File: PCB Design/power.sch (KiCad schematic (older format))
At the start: 18 parts, among them CON2 BARREL_JACK, P1 Power Sel, U1 3.3VREG

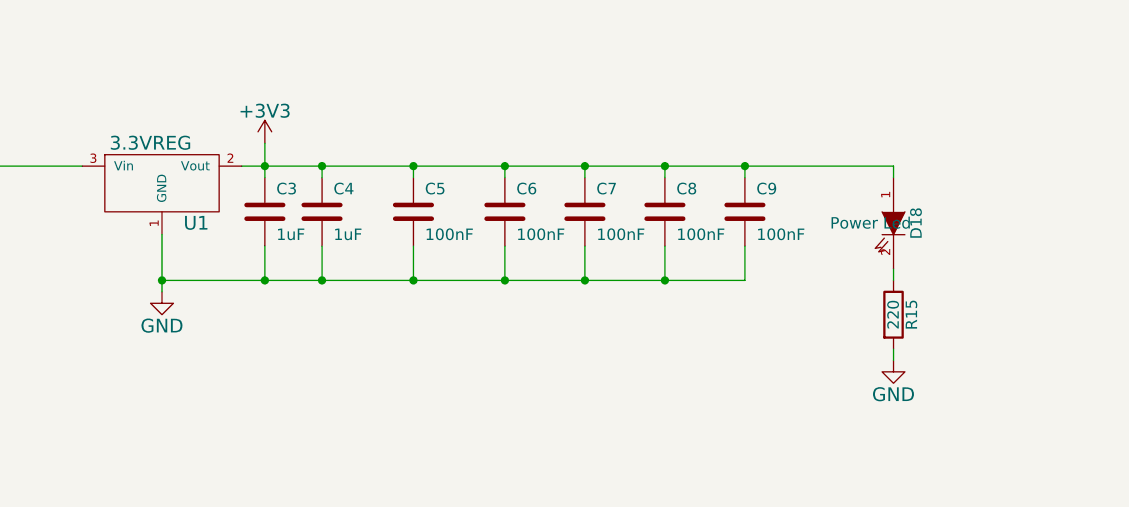
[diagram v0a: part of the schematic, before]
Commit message: Added an additional cap for the MCU, added copper fill on all layers.
Signed-off-by: Kolijn Wolfaardt <kolijn.wolfaardt@gmail.com>
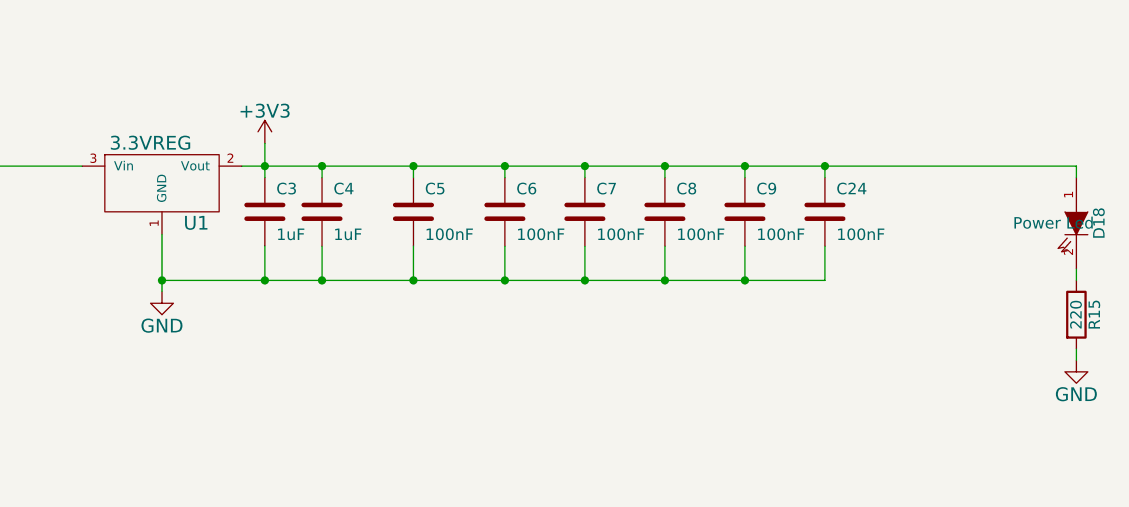
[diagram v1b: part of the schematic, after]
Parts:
- added C24: 100nF, Capacitors_SMD:C_1206, symbol C
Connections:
- net +3V3: now also C24.1
- net GND: now also C24.2
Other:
- moved on the sheet: D18, R15
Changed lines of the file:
@@
 $EndComp
 Wire Wire Line
-	6500 3900 9350 3900
+	6500 3900 10150 3900
 Wire Wire Line
 	6600 3800 6600 3950
@@
 $EndComp
 Wire Wire Line
-	6150 4450 6150 4200
+	6150 4200 6150 4450
 $Comp
 L C C1
@@
 $EndComp
 Wire Wire Line
-	8700 4400 6150 4400
+	6150 4400 9050 4400
 Wire Wire Line
 	6600 4250 6600 4400
@@
 Connection ~ 8000 4400
 Wire Wire Line
-	8700 4250 8700 4400
+	8700 4400 8700 4250
 Connection ~ 8350 4400
 Connection ~ 8350 3900
@@
 L LED D18
 U 1 1 551840ED
-P 9350 4150
-F 0 "D18" H 9350 4250 50  0000 C CNN
-F 1 "Power Led" V 9350 4050 50  0000 C CNN
-F 2 "LEDs:LED-1206" H 9350 4150 60  0001 C CNN
-F 3 "" H 9350 4150 60  0000 C CNN
-	1    9350 4150
+P 10150 4150
+F 0 "D18" H 10150 4250 50  0000 C CNN
+F 1 "Power Led" V 10150 4050 50  0000 C CNN
+F 2 "LEDs:LED-1206" H 10150 4150 60  0001 C CNN
+F 3 "" H 10150 4150 60  0000 C CNN
+	1    10150 4150
 	0    1    1    0
 $EndComp
@@
 L R R15
 U 1 1 55184149
-P 9350 4550
-F 0 "R15" V 9430 4550 50  0000 C CNN
-F 1 "220" V 9350 4550 50  0000 C CNN
-F 2 "Resistors_SMD:R_1206" V 9280 4550 30  0001 C CNN
-F 3 "" H 9350 4550 30  0000 C CNN
-	1    9350 4550
+P 10150 4550
+F 0 "R15" V 10230 4550 50  0000 C CNN
+F 1 "220" V 10150 4550 50  0000 C CNN
+F 2 "Resistors_SMD:R_1206" V 10080 4550 30  0001 C CNN
+F 3 "" H 10150 4550 30  0000 C CNN
+	1    10150 4550
 	1    0    0    -1
 $EndComp
@@
 L GND #PWR08
 U 1 1 551841D4
-P 9350 4750
-F 0 "#PWR08" H 9350 4500 60  0001 C CNN
-F 1 "GND" H 9350 4600 60  0000 C CNN
-F 2 "" H 9350 4750 60  0000 C CNN
-F 3 "" H 9350 4750 60  0000 C CNN
-	1    9350 4750
-	1    0    0    -1
-$EndComp
-Wire Wire Line
-	9350 4700 9350 4750
-Wire Wire Line
-	9350 4400 9350 4350
-Wire Wire Line
-	9350 3900 9350 3950
+P 10150 4750
+F 0 "#PWR08" H 10150 4500 60  0001 C CNN
+F 1 "GND" H 10150 4600 60  0000 C CNN
+F 2 "" H 10150 4750 60  0000 C CNN
+F 3 "" H 10150 4750 60  0000 C CNN
+	1    10150 4750
+	1    0    0    -1
+$EndComp
+Wire Wire Line
+	10150 4700 10150 4750
+Wire Wire Line
+	10150 4400 10150 4350
+Wire Wire Line
+	10150 3900 10150 3950
 Connection ~ 8700 3900
 $Comp
@@
 	2800 2900 3350 2900
 NoConn ~ 2800 3000
+$Comp
+L C C24
+U 1 1 5522DB1C
+P 9050 4100
+F 0 "C24" H 9100 4200 50  0000 L CNN
+F 1 "100nF" H 9100 4000 50  0000 L CNN
+F 2 "Capacitors_SMD:C_1206" H 9088 3950 30  0001 C CNN
+F 3 "" H 9050 4100 60  0000 C CNN
+	1    9050 4100
+	1    0    0    -1
+$EndComp
+Wire Wire Line
+	9050 3950 9050 3900
+Connection ~ 9050 3900
+Wire Wire Line
+	9050 4400 9050 4250
+Connection ~ 8700 4400
 $EndSCHEMATC
